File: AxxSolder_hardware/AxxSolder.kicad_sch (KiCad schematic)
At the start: 95 parts, among them IC1 LTC4440AHMS8E-5#PBF, IC2 STM32G431KBT6, IC3 TMP236AQDBZRQ1, IC4 OPA2333AIDRBR, IC5 STM32G431KBT6, IC6 TPS54302DDCR, J1 Conn_01x07_Male, J4 Conn_01x07_Male, Q2 2N7002NXAKR, U1 PEC11L-4220F-S0015, U2 BSC014N04LS

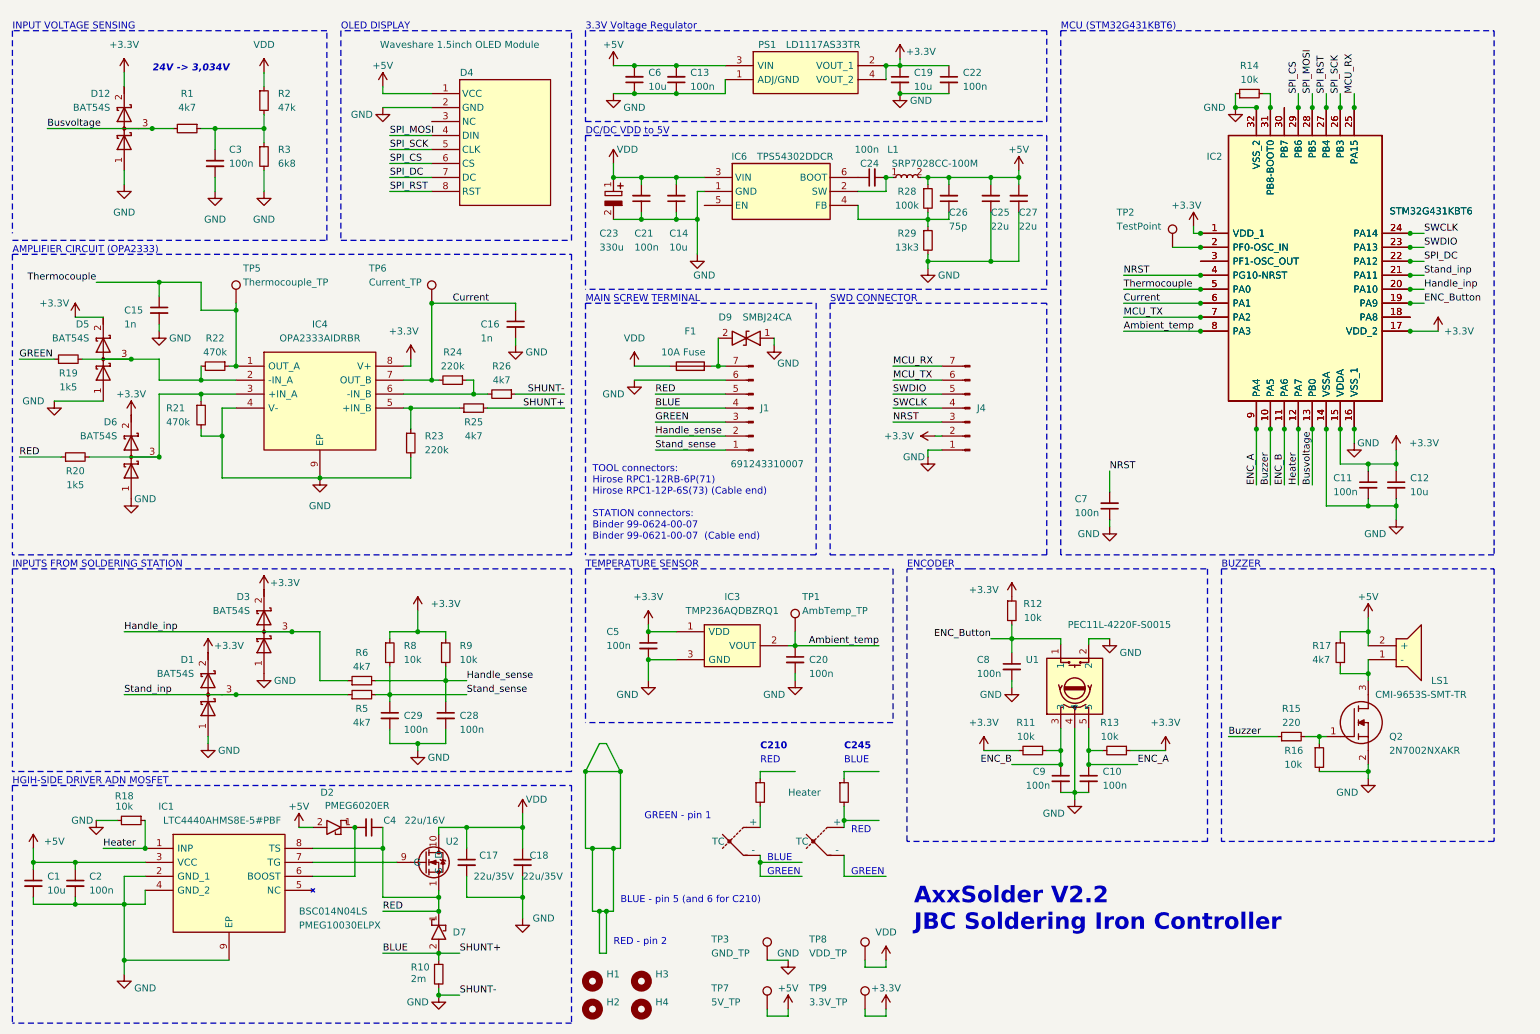
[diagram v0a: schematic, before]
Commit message: update USBC-PD branch
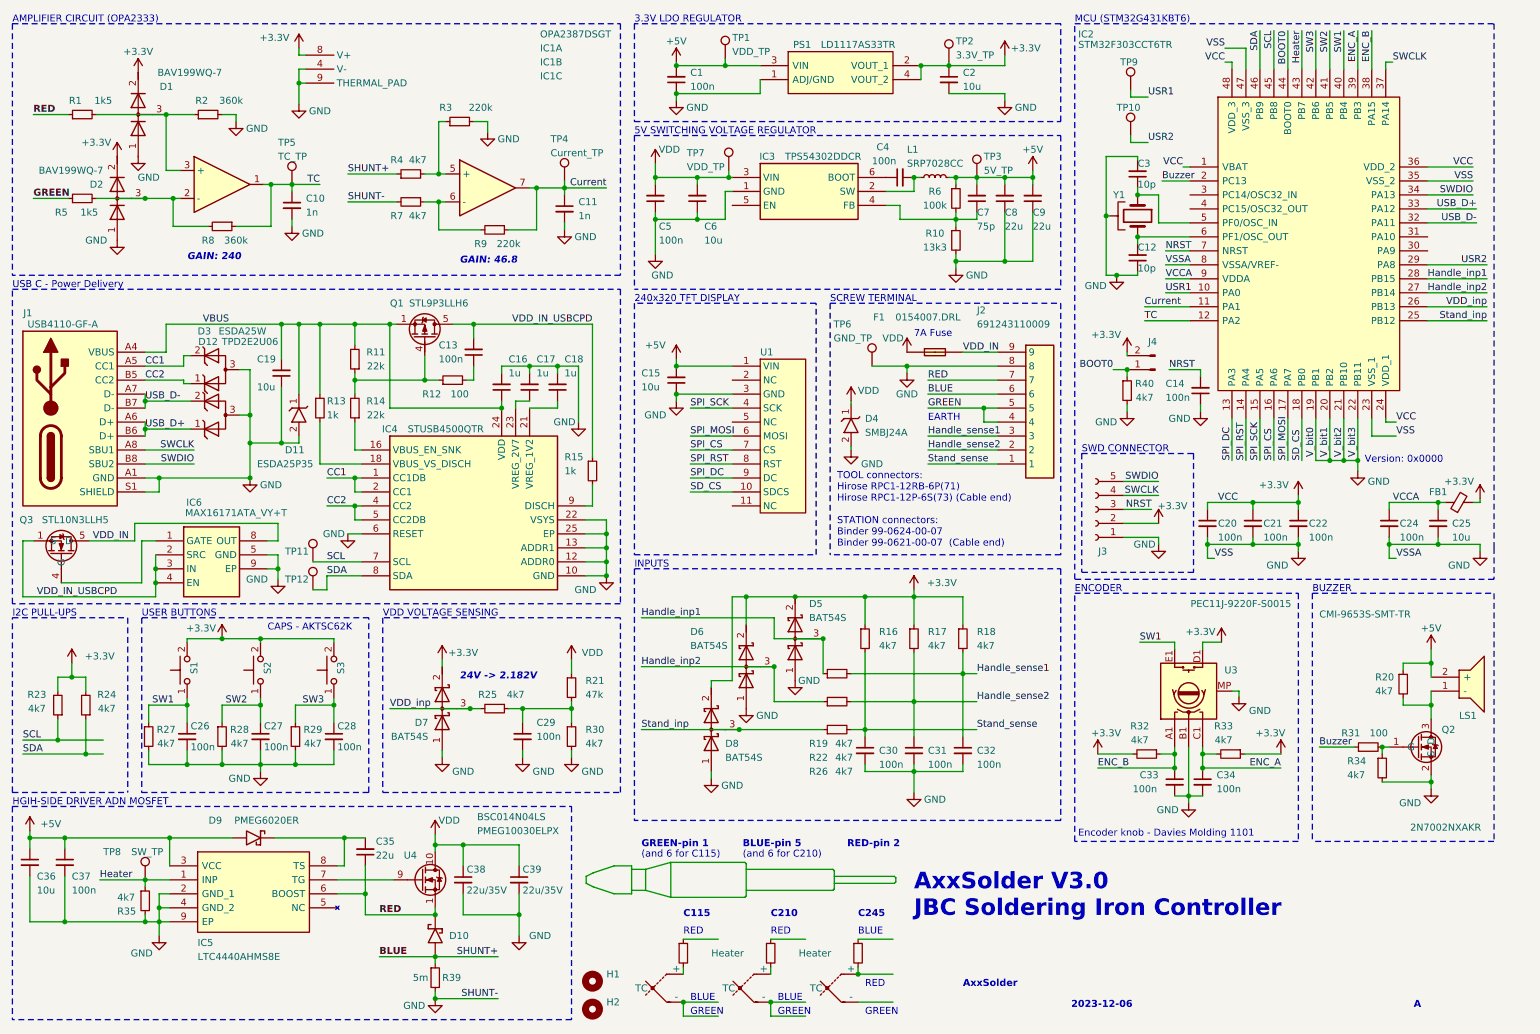
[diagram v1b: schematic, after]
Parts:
- removed C11, C5, C7, C8: 100n, Capacitor_SMD:C_0805_2012Metric, symbol Device:C_Small
- removed C23: 330u, EMZR500ARA331MJA0G:CAPAE1030X1050N, symbol EMZR500ARA331MJA0G:EMZR500ARA331MJA0G
- removed C6: 10u, Capacitor_SMD:C_0805_2012Metric, symbol Device:C_Small
- removed D4: Waveshare 1.5inch OLED Module, 1_5inch-rgb-oled-module_asm-1110:1_5inch-rgb-oled-module_asm-1110, symbol 1_5inch-rgb-oled-module_asm-1110:1_5inch-rgb-oled-module_asm-1110
- removed D6: BAT54S, BAT54S,215:SOT95P230X110-3N, symbol Device:D_Schottky_Dual_Series_AKC
- removed D9: SMBJ24CA, DIOM5436X261N, symbol SMBJ24CA:SMBJ24CA
- removed F1: 10A Fuse, 3557-2:3557-2, symbol Device:Fuse
- removed H3, H4: MountingHole, MountingHole:MountingHole_3mm, symbol Mechanical:MountingHole
- removed IC2: STM32G431KBT6, STM32G431KBT6:QFP80P900X900X160-32N, symbol STM32G431KBT6:STM32G431KBT6
- removed IC3: TMP236AQDBZRQ1, TMP236AQDBZRQ1:SOT95P237X112-3N, symbol TMP236AQDBZRQ1:TMP236AQDBZRQ1
- removed IC4: OPA2333AIDRBR, OPA2333AIDRBR:SON65P300X300X100-9N-D, symbol OPA2333AIDRBR:OPA2333AIDRBR
- removed IC5: STM32G431KBT6, Package_DFN_QFN:UFQFPN-32-1EP_5x5mm_P0.5mm_EP3.5x3.5mm, symbol STM32G431KBT6:STM32G431KBT6
- removed J1: Conn_01x07_Male, 691243310007:691243310007, symbol Connector:Conn_01x07_Male
- removed J4: Conn_01x07_Male, Connector_PinSocket_2.54mm:PinSocket_1x07_P2.54mm_Vertical, symbol Connector:Conn_01x07_Male
- removed R10: 2m, WSLP25122L500FEA:RESC6432X89N, symbol Device:R_Small
- removed R21: 470k, Resistor_SMD:R_0805_2012Metric, symbol Device:R_Small
- removed TP1: AmbTemp_TP, TestPoint:TestPoint_THTPad_D1.0mm_Drill0.5mm, symbol Connector:TestPoint
- removed TP2: TestPoint, TestPoint:TestPoint_Pad_D1.0mm, symbol Connector:TestPoint
- removed U1: PEC11L-4220F-S0015, PEC11L-4220F-S0015:PEC11L4220FS0015, symbol PEC11L-4220F-S0015:PEC11L-4220F-S0015
- added C13, C14, C21, C24, C26, C27, C28, C32: 100n, Capacitor_SMD:C_0603_1608Metric, symbol Device:C_Small
- added C15, C19, C25: 10u, Capacitor_SMD:C_0603_1608Metric, symbol Device:C_Small
- added C16, C17, C18: 1u, Capacitor_SMD:C_0603_1608Metric, symbol Device:C_Small
- added C3: 10p, Capacitor_SMD:C_0603_1608Metric, symbol Device:C_Small
- added D1, D2: BAV199WQ-7, footprints:SOT65P210X110-3N, symbol BAV199WQ-7:BAV199WQ-7
- added D11: ESDA25P35, footprints:ESDA25P351U1M, symbol ESDA25P35-1U1M:ESDA25P35-1U1M
- added D12: TPD2E2U06, footprints:SOT95P237X95-3N, symbol TPD2E2U06QDBZRQ1:TPD2E2U06QDBZRQ1
- added D3: ESDA25W, footprints:SOT65P210X110-3N, symbol ESDA25W:ESDA25W
- added D4: SMBJ24A, footprints:DIOM5436X261N, symbol SMBJ24A:SMBJ24A
- added F1: 0154007.DRL, footprints:0154100DR, symbol 0154007_DRL:0154007.DRL
- added FB1: BLM18HE601SN1D, Resistor_SMD:R_0603_1608Metric, symbol BLM18HE601SN1D:BLM18HE601SN1D
- added IC1: OPA2387DSGT, footprints:SON50P200X200X80-9N, symbol OPA2387DSGT:OPA2387DSGT
- added IC2: STM32F303CCT6TR, footprints:QFP50P900X900X160-48N, symbol STM32F303CCT6TR:STM32F303CCT6TR
- added IC4: STUSB4500QTR, footprints:QFN50P400X400X100-25N-D, symbol STUSB4500QTR:STUSB4500QTR
- added IC6: MAX16171ATA_VY+T, SON50P300X200X80-9N, symbol MAX16171ATA_VY+T:MAX16171ATA_VY+T
- added J1: USB4110-GF-A, footprints:USB4110GFA, symbol USB4110-GF-A:USB4110-GF-A
- added J2: 691243110009, footprints:691243110009, symbol 691243110009:691243110009
- added J3: Conn_01x05_Socket, Connector_PinSocket_2.54mm:PinSocket_1x05_P2.54mm_Vertical, symbol Connector:Conn_01x05_Socket
- added J4: Conn_01x02_Pin, Connector_PinHeader_1.27mm:PinHeader_1x02_P1.27mm_Vertical, symbol Connector:Conn_01x02_Pin
- added Q1: STL9P3LLH6, footprints:STL20N6F7, symbol STL9P3LLH6:STL9P3LLH6
- added Q3: STL10N3LLH5, STL10N3LLH5, symbol STL10N3LLH5:STL10N3LLH5
- added R11: 22k, Resistor_SMD:R_0603_1608Metric, symbol Device:R_Small
- added R13: 1k, Resistor_SMD:R_0603_1608Metric, symbol Device:R_Small
- added R18, R19, R23, R24, R27, R28, R29, R40: 4k7, Resistor_SMD:R_0603_1608Metric, symbol Device:R_Small
- added R2: 360k, Resistor_SMD:R_0603_1608Metric, symbol Device:R_Small
- added R31: 100, Resistor_SMD:R_0603_1608Metric, symbol Device:R_Small
- added R36: Heater, symbol Device:R_Small
- added R39: 5m, footprints:RESC6432X89N, symbol WSLP25125L000FEA:WSLP25125L000FEA
- added S1, S2, S3: ADTSM644KVTR, footprints:ADTSM644KVTR, symbol ADTSM644KVTR:ADTSM644KVTR
- added TC1: TC, symbol Device:Thermocouple
- added TP10, TP11, TP12, TP9: DIAG_TP, TestPoint:TestPoint_Pad_D1.0mm, symbol Connector:TestPoint
- added TP7: VDD_TP, TestPoint:TestPoint_THTPad_D1.0mm_Drill0.5mm, symbol Connector:TestPoint
- added TP8: SW_TP, TestPoint:TestPoint_Pad_D1.0mm, symbol Connector:TestPoint
- added U1: ~, footprints:Adafruit_240x320_TFT, symbol Adafruit_240x320_TFT:Adafruit_240x320_TFT
- added U3: PEC11J-9220F-S0015, footprints:PEC11J9220FS0015, symbol PEC11J-9220F-S0015:PEC11J-9220F-S0015
- added Y1: NX2016SA-32M-EXS00A-CS06465, footprints:NX2016SA32MEXS00ACS06465, symbol NX2016SA-32M-EXS00A-CS06465:NX2016SA-32M-EXS00A-CS06465
- C1: renamed from C13; footprint Capacitor_SMD:C_0805_2012Metric -> Capacitor_SMD:C_0603_1608Metric; Manufacturer_Name (none) -> KEMET; Manufacturer_Part_Number (none) -> C0603C104J5RACTU
- C10: renamed from C15; footprint Capacitor_SMD:C_0805_2012Metric -> Capacitor_SMD:C_0603_1608Metric; Manufacturer_Name (none) -> KEMET; Manufacturer_Part_Number (none) -> C0603C102K3GAC
- C11: renamed from C16; footprint Capacitor_SMD:C_0805_2012Metric -> Capacitor_SMD:C_0603_1608Metric; Manufacturer_Name (none) -> KEMET; Manufacturer_Part_Number (none) -> C0603C102K3GAC
- C12: value 10u -> 10p; footprint Capacitor_SMD:C_0805_2012Metric -> Capacitor_SMD:C_0603_1608Metric; Manufacturer_Name (none) -> KEMET; Manufacturer_Part_Number (none) -> C0603C100J5GAC
- C2: renamed from C19; footprint Capacitor_SMD:C_0805_2012Metric -> Capacitor_SMD:C_0603_1608Metric; Manufacturer_Name (none) -> Murata Electronics; Manufacturer_Part_Number (none) -> GRM188R6YA106MA73J
- C20, C22: footprint Capacitor_SMD:C_0805_2012Metric -> Capacitor_SMD:C_0603_1608Metric; Manufacturer_Name (none) -> KEMET; Manufacturer_Part_Number (none) -> C0603C104J5RACTU
- C29: renamed from C3; footprint Capacitor_SMD:C_0805_2012Metric -> Capacitor_SMD:C_0603_1608Metric; Manufacturer_Name (none) -> KEMET; Manufacturer_Part_Number (none) -> C0603C104J5RACTU
- C30: renamed from C29; footprint Capacitor_SMD:C_0805_2012Metric -> Capacitor_SMD:C_0603_1608Metric; Manufacturer_Name (none) -> KEMET; Manufacturer_Part_Number (none) -> C0603C104J5RACTU
- C31: renamed from C28; footprint Capacitor_SMD:C_0805_2012Metric -> Capacitor_SMD:C_0603_1608Metric; Manufacturer_Name (none) -> KEMET; Manufacturer_Part_Number (none) -> C0603C104J5RACTU
- C33: renamed from C9; footprint Capacitor_SMD:C_0805_2012Metric -> Capacitor_SMD:C_0603_1608Metric; Manufacturer_Name (none) -> KEMET; Manufacturer_Part_Number (none) -> C0603C104J5RACTU
- C34: renamed from C10; footprint Capacitor_SMD:C_0805_2012Metric -> Capacitor_SMD:C_0603_1608Metric; Manufacturer_Name (none) -> KEMET; Manufacturer_Part_Number (none) -> C0603C104J5RACTU
- C35: renamed from C4; value 22u/16V -> 22u; Manufacturer_Name (none) -> Samsung Electro-Mechanics; Manufacturer_Part_Number (none) -> CL31A226MOCLNNC
- C36: renamed from C1; footprint Capacitor_SMD:C_0805_2012Metric -> Capacitor_SMD:C_0603_1608Metric; Manufacturer_Name (none) -> Murata Electronics; Manufacturer_Part_Number (none) -> GRM188R6YA106MA73J
- C37: renamed from C2; footprint Capacitor_SMD:C_0805_2012Metric -> Capacitor_SMD:C_0603_1608Metric; Manufacturer_Name (none) -> KEMET; Manufacturer_Part_Number (none) -> C0603C104J5RACTU
- C38: renamed from C17; Manufacturer_Name (none) -> TDK; Manufacturer_Part_Number (none) -> C3216X5R1V226M160AC
- C39: renamed from C18; Manufacturer_Name (none) -> TDK; Manufacturer_Part_Number (none) -> C3216X5R1V226M160AC
- C4: renamed from C24; footprint Capacitor_SMD:C_0805_2012Metric -> Capacitor_SMD:C_0603_1608Metric; Manufacturer_Name (none) -> KEMET; Manufacturer_Part_Number (none) -> C0603C104J5RACTU
- C5: renamed from C21; footprint Capacitor_SMD:C_0805_2012Metric -> Capacitor_SMD:C_0603_1608Metric; Manufacturer_Name (none) -> KEMET; Manufacturer_Part_Number (none) -> C0603C104J5RACTU
- C6: renamed from C14; footprint Capacitor_SMD:C_0805_2012Metric -> Capacitor_SMD:C_0603_1608Metric; Manufacturer_Name (none) -> Murata Electronics; Manufacturer_Part_Number (none) -> GRM188R6YA106MA73J
- C7: renamed from C26; footprint Capacitor_SMD:C_0805_2012Metric -> Capacitor_SMD:C_0603_1608Metric; Manufacturer_Name (none) -> KEMET; Manufacturer_Part_Number (none) -> C0603C750K5HACTU
- C8: renamed from C25; Manufacturer_Name (none) -> Samsung Electro-Mechanics; Manufacturer_Part_Number (none) -> CL31A226MOCLNNC
- C9: renamed from C27; Manufacturer_Name (none) -> Samsung Electro-Mechanics; Manufacturer_Part_Number (none) -> CL31A226MOCLNNC
- D10: renamed from D7; footprint PMEG10030ELPX:SODFL4725X110N -> footprints:SODFL4725X110N
- D5: footprint BAT54S,215:SOT95P230X110-3N -> footprints:SOT95P230X110-3N; Manufacturer_Name (none) -> Diotec Semiconductor; Manufacturer_Part_Number (none) -> BAT54S; Mouser Part Number (none) -> 637-BAT54S; Mouser Price/Stock (none) -> https://www.mouser.co.uk/ProductDetail/Diotec-Semiconductor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
- D6: renamed from D3; footprint BAT54S,215:SOT95P230X110-3N -> footprints:SOT95P230X110-3N; Manufacturer_Name (none) -> Diotec Semiconductor; Manufacturer_Part_Number (none) -> BAT54S; Mouser Part Number (none) -> 637-BAT54S; Mouser Price/Stock (none) -> https://www.mouser.co.uk/ProductDetail/Diotec-Semiconductor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
- D7: renamed from D12; footprint BAT54S,215:SOT95P230X110-3N -> footprints:SOT95P230X110-3N; Manufacturer_Name (none) -> Diotec Semiconductor; Manufacturer_Part_Number (none) -> BAT54S; Mouser Part Number (none) -> 637-BAT54S; Mouser Price/Stock (none) -> https://www.mouser.co.uk/ProductDetail/Diotec-Semiconductor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
- D8: renamed from D1; footprint BAT54S,215:SOT95P230X110-3N -> footprints:SOT95P230X110-3N; Manufacturer_Name (none) -> Diotec Semiconductor; Manufacturer_Part_Number (none) -> BAT54S; Mouser Part Number (none) -> 637-BAT54S; Mouser Price/Stock (none) -> https://www.mouser.co.uk/ProductDetail/Diotec-Semiconductor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
- D9: renamed from D2; footprint PMEG6020ER,115:PMEG6020ER115 -> footprints:PMEG6020ER115
- H1, H2: footprint MountingHole:MountingHole_3mm -> MountingHole:MountingHole_2.5mm; Assembly Comment (none) -> N/A; now left out of the parts list
- IC3: renamed from IC6; footprint TPS54302DDCR:SOT95P280X110-6N -> footprints:SOT95P280X110-6N
- IC5: renamed from IC1; value LTC4440AHMS8E-5#PBF -> LTC4440AHMS8E; footprint LTC4440AHMS8E-5#PBF:SOP65P490X110-9N -> footprints:SOP65P490X110-9N
- L1: value SRP7028CC-100M -> SRP7028CC; footprint SRP7028CC-100M:INDPM7366X300N -> footprints:INDPM7366X300N; Mouser Part Number (none) -> 652-SRP7028CC-100M
- LS1: footprint CMI-9653S-SMT-TR:CMI9653SSMTTR -> footprints:CMI9653SSMTTR
- PS1: footprint SOT230P700X190-4N -> footprints:SOT230P700X190-4N
- Q2: footprint 2N7002NXAKR:SOT95P230X110-3N -> SOT95P230X110-3N
- R1: renamed from R20; footprint Resistor_SMD:R_0805_2012Metric -> Resistor_SMD:R_0603_1608Metric; Manufacturer_Name (none) -> Panasonic; Manufacturer_Part_Number (none) -> ERJ-H3ED1501V; Mouser Part Number (none) -> 667-ERJ-H3ED1501V
- R10: renamed from R29; footprint Resistor_SMD:R_0805_2012Metric -> Resistor_SMD:R_0603_1608Metric; Manufacturer_Name (none) -> Panasonic; Manufacturer_Part_Number (none) -> ERJ-PB3B1332V; Mouser Part Number (none) -> 667-ERJ-PB3B1332V
- R12: value 10k -> 100; footprint Resistor_SMD:R_0805_2012Metric -> Resistor_SMD:R_0603_1608Metric; Manufacturer_Name (none) -> Panasonic; Manufacturer_Part_Number (none) -> ERJ-P03F1000V; Mouser Part Number (none) -> 667-ERJ-P03F1000V
- R14: value 10k -> 22k; footprint Resistor_SMD:R_0805_2012Metric -> Resistor_SMD:R_0603_1608Metric; Manufacturer_Name (none) -> Panasonic; Manufacturer_Part_Number (none) -> ERJ-UP3J223V; Mouser Part Number (none) -> 667-ERJ-UP3J223V
- R15: value 220 -> 1k; footprint Resistor_SMD:R_0805_2012Metric -> Resistor_SMD:R_0603_1608Metric; Manufacturer_Name (none) -> Panasonic; Manufacturer_Part_Number (none) -> ERJ-H3EF1001V; Mouser Part Number (none) -> 667-ERJ-H3EF1001V
- R16: renamed from R8; value 10k -> 4k7; footprint Resistor_SMD:R_0805_2012Metric -> Resistor_SMD:R_0603_1608Metric; Manufacturer_Name (none) -> Panasonic; Manufacturer_Part_Number (none) -> ERJ-3RBD4701V; Mouser Part Number (none) -> 667-ERJ-3RBD4701V
- R17: renamed from R9; value 10k -> 4k7; footprint Resistor_SMD:R_0805_2012Metric -> Resistor_SMD:R_0603_1608Metric; Manufacturer_Name (none) -> Panasonic; Manufacturer_Part_Number (none) -> ERJ-3RBD4701V; Mouser Part Number (none) -> 667-ERJ-3RBD4701V
- R20: renamed from R17; footprint Resistor_SMD:R_0805_2012Metric -> Resistor_SMD:R_0603_1608Metric; Manufacturer_Name (none) -> Panasonic; Manufacturer_Part_Number (none) -> ERJ-3RBD4701V; Mouser Part Number (none) -> 667-ERJ-3RBD4701V
- R21: renamed from R2; footprint Resistor_SMD:R_0805_2012Metric -> Resistor_SMD:R_0603_1608Metric; Manufacturer_Name (none) -> Panasonic; Manufacturer_Part_Number (none) -> ERJ-H3ED4702V; Mouser Part Number (none) -> 667-ERJ-H3ED4702V
- R22: renamed from R6; footprint Resistor_SMD:R_0805_2012Metric -> Resistor_SMD:R_0603_1608Metric; Manufacturer_Name (none) -> Panasonic; Manufacturer_Part_Number (none) -> ERJ-3RBD4701V; Mouser Part Number (none) -> 667-ERJ-3RBD4701V
- R25: renamed from R1; footprint Resistor_SMD:R_0805_2012Metric -> Resistor_SMD:R_0603_1608Metric; Manufacturer_Name (none) -> Panasonic; Manufacturer_Part_Number (none) -> ERJ-3RBD4701V; Mouser Part Number (none) -> 667-ERJ-3RBD4701V
- R26: renamed from R5; footprint Resistor_SMD:R_0805_2012Metric -> Resistor_SMD:R_0603_1608Metric; Manufacturer_Name (none) -> Panasonic; Manufacturer_Part_Number (none) -> ERJ-3RBD4701V; Mouser Part Number (none) -> 667-ERJ-3RBD4701V
- R3: renamed from R23; footprint Resistor_SMD:R_0805_2012Metric -> Resistor_SMD:R_0603_1608Metric; Manufacturer_Name (none) -> Panasonic; Manufacturer_Part_Number (none) -> ERJ-3RED2203V; Mouser Part Number (none) -> 667-ERJ-3RED2203V
- R30: renamed from R3; value 6k8 -> 4k7; footprint Resistor_SMD:R_0805_2012Metric -> Resistor_SMD:R_0603_1608Metric; Manufacturer_Name (none) -> Panasonic; Manufacturer_Part_Number (none) -> ERJ-3RBD4701V; Mouser Part Number (none) -> 667-ERJ-3RBD4701V
- R32: renamed from R11; value 10k -> 4k7; footprint Resistor_SMD:R_0805_2012Metric -> Resistor_SMD:R_0603_1608Metric; Manufacturer_Name (none) -> Panasonic; Manufacturer_Part_Number (none) -> ERJ-3RBD4701V; Mouser Part Number (none) -> 667-ERJ-3RBD4701V
- R33: renamed from R13; value 10k -> 4k7; footprint Resistor_SMD:R_0805_2012Metric -> Resistor_SMD:R_0603_1608Metric; Manufacturer_Name (none) -> Panasonic; Manufacturer_Part_Number (none) -> ERJ-3RBD4701V; Mouser Part Number (none) -> 667-ERJ-3RBD4701V
- R34: renamed from R16; value 10k -> 4k7; footprint Resistor_SMD:R_0805_2012Metric -> Resistor_SMD:R_0603_1608Metric; Manufacturer_Name (none) -> Panasonic; Manufacturer_Part_Number (none) -> ERJ-3RBD4701V; Mouser Part Number (none) -> 667-ERJ-3RBD4701V
- R35: renamed from R18; value 10k -> 4k7; footprint Resistor_SMD:R_0805_2012Metric -> Resistor_SMD:R_0603_1608Metric; Manufacturer_Name (none) -> Panasonic; Manufacturer_Part_Number (none) -> ERJ-3RBD4701V; Mouser Part Number (none) -> 667-ERJ-3RBD4701V
- R37: renamed from R4; Assembly Comment (none) -> N/A
- R38: renamed from R7; Assembly Comment (none) -> N/A
- R4: renamed from R25; footprint Resistor_SMD:R_0805_2012Metric -> Resistor_SMD:R_0603_1608Metric; Manufacturer_Name (none) -> Panasonic; Manufacturer_Part_Number (none) -> ERJ-3RBD4701V; Mouser Part Number (none) -> 667-ERJ-3RBD4701V
- R5: renamed from R19; footprint Resistor_SMD:R_0805_2012Metric -> Resistor_SMD:R_0603_1608Metric; Manufacturer_Name (none) -> Panasonic; Manufacturer_Part_Number (none) -> ERJ-H3ED1501V; Mouser Part Number (none) -> 667-ERJ-H3ED1501V
- R6: renamed from R28; footprint Resistor_SMD:R_0805_2012Metric -> Resistor_SMD:R_0603_1608Metric; Manufacturer_Name (none) -> Panasonic; Manufacturer_Part_Number (none) -> ERJ-UP3D1003V; Mouser Part Number (none) -> 667-ERJ-UP3D1003V
- R7: renamed from R26; footprint Resistor_SMD:R_0805_2012Metric -> Resistor_SMD:R_0603_1608Metric; Manufacturer_Name (none) -> Panasonic; Manufacturer_Part_Number (none) -> ERJ-3RBD4701V; Mouser Part Number (none) -> 667-ERJ-3RBD4701V
- R8: renamed from R22; value 470k -> 360k; footprint Resistor_SMD:R_0805_2012Metric -> Resistor_SMD:R_0603_1608Metric; Manufacturer_Name (none) -> Panasonic; Manufacturer_Part_Number (none) -> ERJ-3RED3603V; Mouser Part Number (none) -> 667-ERJ-3RED3603V
- R9: renamed from R24; footprint Resistor_SMD:R_0805_2012Metric -> Resistor_SMD:R_0603_1608Metric; Manufacturer_Name (none) -> Panasonic; Manufacturer_Part_Number (none) -> ERJ-3RED2203V; Mouser Part Number (none) -> 667-ERJ-3RED2203V
- TC2: renamed from TC1; Assembly Comment (none) -> N/A
- TC3: renamed from TC2; Assembly Comment (none) -> N/A
- TP1: renamed from TP8; Assembly Comment (none) -> N/A; now left out of the parts list
- TP2: renamed from TP9; Assembly Comment (none) -> N/A; now left out of the parts list
- TP3: renamed from TP7; Assembly Comment (none) -> N/A; now left out of the parts list
- TP4: renamed from TP6; Assembly Comment (none) -> N/A; now left out of the parts list
- TP5: value Thermocouple_TP -> TC_TP; Assembly Comment (none) -> N/A; now left out of the parts list
- TP6: renamed from TP3; Assembly Comment (none) -> N/A; now left out of the parts list
- U4: renamed from U2; footprint BSC014N04LS:BSC014N04LS -> footprints:BSC014N04LS; Manufacturer_Name (none) -> Infineon Technologies; Manufacturer_Part_Number (none) -> BSC014N04LSATMA1; Mouser Part Number (none) -> 726-BSC014N04LSATMA1
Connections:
- net Ambient_temp is gone; now on net +3.3V: C20.1
- net +3.3V: now also C21.1, D1.2, D2.2, FB1.2, IC1.8 (V+), IC2.1 (VBAT), IC2.24 (VDD_1), IC2.36 (VDD_2), IC2.48 (VDD_3), J3.2 (Pin_2), J4.2 (Pin_2), R18.1, R23.2, R24.2, S1.2, S2.2, S3.2, U3.D1; no longer C12.1, R12.1
- net +5V: now also TP1.1, C15.2, U1.1 (VIN)
- net BLUE: now also R4.1, J2.6, R39.1; no longer R4.2
- net Buzzer: now also IC2.2 (PC13), R31.1; no longer R15.1
- net Current: now also R9.1, IC1.7, IC2.11 (PA1); no longer R9.2
- net ENC_A: now also IC2.39 (PB3), U3.C1
- net ENC_B: now also IC2.38 (PA15), U3.A1
- net GND: now also C12.1, R7.2, C14.1, C15.1, C16.2, C17.2, C18.2, C19.1, C21.2, C24.2, C25.2, C26.2, C27.2, C28.2, C3.2, C32.2, D1.1, D11.2 (A), D12.3, D2.1, D3.3, D4.2 (A), IC1.4 (V-), IC1.9 (THERMAL_PAD), IC2.19 (PB1), IC2.20 (PB2), IC2.21 (PB10), IC2.22 (PB11), IC2.23 (VSS_1), IC2.35 (VSS_2), IC2.47 (VSS_3), IC2.8 (VSSA/VREF-), IC4.10 (GND), IC4.12 (ADDR0), IC4.13 (ADDR1), IC4.22 (VSYS), IC4.25 (EP), IC4.6 (RESET), IC6.5 (GND), IC6.9 (EP), J1.A1 (GND), J1.A12 (GND), J1.B1 (GND), J1.B12 (GND), J1.S1 (SHIELD), J2.8, J3.1 (Pin_1), R2.2, R27.2, R28.2, R29.2, R39.2, R40.2, U1.3 (GND), U3.B1, U3.MP, Y1.2; no longer C12.2, R14.1, R7.1
- net GREEN: now also J2.4, J2.5
- net Heater: now also IC2.43 (PB7), TP8.1
- net NRST: now also C14.2, IC2.7 (NRST), J3.3 (Pin_3)
- net RED: now also IC5.6 (BOOST), J2.7; no longer IC5.8 (TS)
- net SPI_CS: now also IC2.16 (PA6), U1.7 (CS)
- net SPI_DC: now also IC2.13 (PA3), U1.9 (DC)
- net SPI_MOSI: now also IC2.17 (PA7), U1.6 (MOSI)
- net SPI_RST: now also IC2.14 (PA4), U1.8 (RST)
- net SPI_SCK: now also IC2.15 (PA5), U1.4 (SCK)
- net SWCLK: now also IC2.37 (PA14), J1.A8 (SBU1), J3.4 (Pin_4)
- net SWDIO: now also IC2.34 (PA13), J1.B8 (SBU2), J3.5 (Pin_5)
- net Stand_inp: now also IC2.25 (PB12)
- net Stand_sense: now also J2.1
- net VDD: now also D4.1 (K), F1.1, TP7.1; no longer TP1.1
- net at Q2.1 (G), R34.1: now also R31.2; no longer R15.2
- net at R5.2, R8.2: now also D2.3, IC1.2 (-); no longer D5.3 (common)
- net at R1.2: now also D1.3, IC1.3 (+), R2.1
- net at R3.1: now also R4.2, IC1.5 (+); no longer R4.1
- net at R14.2: now also R12.1, Q1.4 (G), R11.1
- net at C35.2, D9.1: now also IC5.8 (TS); no longer IC5.6 (BOOST)
- net Busvoltage renamed VDD_inp
- net VDD_inp: now also IC2.26 (PB13)
- net ENC_Button: no longer names the net of R12.2
- net ENC_Button: now also C13.1
- net Handle_inp renamed Handle_inp2
- net Handle_inp2: now also IC2.27 (PB14)
- net Handle_sense renamed Handle_sense2
- net Handle_sense2: now also J2.2
- net Thermocouple renamed TC
- net TC: now also IC1.1, IC2.12 (PA2)
- new net: R36.2, TC1.1 (+)
- new net: IC4.18 (VBUS_VS_DISCH), R13.2
- new net: IC6.1 (GATE), Q3.4 (G)
- new net: C17.1, IC4.23 (VREG_2V7)
- new net: IC1.6 (-), R7.1, R9.2
- new net: C12.2, IC2.6 (PF1/OSC_OUT), Y1.3
- new net: C3.1, IC2.5 (PF0/OSC_IN), Y1.1
- new net: C18.1, IC4.21 (VREG_1V2)
- new net: IC4.16 (VBUS_EN_SNK), R14.1
- new net: IC4.9 (DISCH), R15.2
- new net BOOT0: IC2.44 (BOOT0), J4.1 (Pin_1), R40.1
- new net CC1: D3.2, IC4.1 (CC1DB), IC4.2 (CC1), J1.A5 (CC1)
- new net CC2: D3.1, IC4.4 (CC2), IC4.5 (CC2DB), J1.B5 (CC2)
- new net Handle_inp1: D5.3 (common), IC2.28 (PB15), R19.1
- new net Handle_sense1: C32.1, J2.3, R18.2, R19.2
- new net SCL: IC2.45 (PB8), IC4.7 (SCL), R23.1, TP11.1
- new net SDA: IC2.46 (PB9), IC4.8 (SDA), R24.1, TP12.1
- new net SD_CS: IC2.18 (PB0), U1.10 (SDCS)
- new net SW1: C26.1, IC2.40 (PB4), R27.1, S1.1, U3.E1
- new net SW2: C27.1, IC2.41 (PB5), R28.1, S2.1
- new net SW3: C28.1, IC2.42 (PB6), R29.1, S3.1
- new net USB_D+: D12.1, IC2.33 (PA12), J1.A6 (D+), J1.B6 (D+)
- new net USB_D-: D12.2, IC2.32 (PA11), J1.A7 (D-), J1.B7 (D-)
- new net USR1: IC2.10 (PA0), TP9.1
- new net USR2: IC2.29 (PA8), TP10.1
- new net VBUS: C16.1, C19.2, D11.1 (K), IC4.24 (VDD), J1.A4 (VBUS), J1.A9 (VBUS), J1.B4 (VBUS), J1.B9 (VBUS), Q1.1 (S), R11.2, R13.1
- new net VCCA: C24.1, C25.1, FB1.1, IC2.9 (VDDA)
- new net VDD_IN: F1.2, IC6.8 (OUT), J2.9, Q3.5 (D)
- new net VDD_IN_USBCPD: C13.2, IC6.2 (SRC), IC6.3 (IN), IC6.4 (EN), Q1.5 (D), Q3.1 (S), R15.1
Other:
- note added: "(and 6 for C115)"
- note added: "(and 6 for C210)"
- note added: "2023-12-06"
- note added: "240x320 TFT DISPLAY"
- note added: "24V -> 2.182V"
- note added: "3.3V LDO REGULATOR"
- note added: "5V SWITCHING VOLTAGE REGULATOR"
- note added: "7A Fuse"
- note added: "A"
- note added: "AxxSolder"
- note added: "AxxSolder V3.0 JBC Soldering Iron Controller"
- note added: "BLUE-pin 5"
- note added: "C115"
- note added: "CAPS - AKTSC62K"
- note added: "EARTH"
- note added: "Encoder knob - Davies Molding 1101"
- note added: "GAIN: 240"
- note added: "GAIN: 46.8"
- note added: "GREEN-pin 1"
- note added: "I2C PULL-UPS"
- note added: "INPUTS"
- note added: "RED-pin 2"
- note added: "SCREW TERMINAL"
- note added: "USB C - Power Delivery"
- note added: "USER BUTTONS"
- note added: "VDD VOLTAGE SENSING"
- note added: "Version: 0x0000"
- note removed: "24V -> 3,034V"
- note removed: "3.3V Voltage Regulator"
- note removed: "AxxSolder V2.2 JBC Soldering Iron Controller"
- note removed: "BLUE - pin 5 (and 6 for C210)"
- note removed: "DC/DC VDD to 5V"
- note removed: "GREEN - pin 1"
- note removed: "INPUT VOLTAGE SENSING"
- note removed: "INPUTS FROM SOLDERING STATION"
- note removed: "MAIN SCREW TERMINAL"
- note removed: "OLED DISPLAY"
- note removed: "RED - pin 2"
- note removed: "TEMPERATURE SENSOR"
- moved on the sheet: C10, C11, C2, C29, C30, C31, C33, C34, C35, C36, C37, C38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

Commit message: updates in hardware and software
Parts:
- removed C12, C3: 10p, Capacitor_SMD:C_0603_1608Metric, symbol Device:C_Small
- removed C15: 10u, Capacitor_SMD:C_0603_1608Metric, symbol Device:C_Small
- removed D10: PMEG10030ELPX, footprints:SODFL4725X110N, symbol PMEG10030ELPX:PMEG10030ELPX
- removed IC2: STM32F303CCT6TR, footprints:QFP50P900X900X160-48N, symbol STM32F303CCT6TR:STM32F303CCT6TR
- removed J4: Conn_01x02_Pin, Connector_PinHeader_1.27mm:PinHeader_1x02_P1.27mm_Vertical, symbol Connector:Conn_01x02_Pin
- removed R40: 4k7, Resistor_SMD:R_0603_1608Metric, symbol Device:R_Small
- removed Y1: NX2016SA-32M-EXS00A-CS06465, footprints:NX2016SA32MEXS00ACS06465, symbol NX2016SA-32M-EXS00A-CS06465:NX2016SA-32M-EXS00A-CS06465
- added D13: PMEG6020ER, footprints:PMEG6020ER115, symbol PMEG6020ER_115:PMEG6020ER,115
- added IC7: STM32G431CBT6, QFP50P900X900X160-48N, symbol STM32G431CBT6:STM32G431CBT6
- added R41: 22k, Resistor_SMD:R_0603_1608Metric, symbol Device:R_Small
- added TP13, TP15: DIAG_TP, TestPoint:TestPoint_Pad_D1.0mm, symbol Connector:TestPoint
- added TP14: TC_TP, TestPoint:TestPoint_Pad_D1.0mm, symbol Connector:TestPoint
- C16, C17, C18: value 1u -> 10u
- IC6: footprint SON50P300X200X80-9N -> footprints:SON50P300X200X80-9N
- Q2: footprint SOT95P230X110-3N -> footprints:SOT95P230X110-3N
- Q3: footprint STL10N3LLH5 -> footprints:STL10N3LLH5
- R10: value 13k3 -> 22k
- R13, R15: value 1k -> 1k5
- R21: value 47k -> 22k
- R6: value 100k -> 220k
- TP1: value VDD_TP -> DIAG_TP; footprint TestPoint:TestPoint_THTPad_D1.0mm_Drill0.5mm -> TestPoint:TestPoint_Pad_D1.0mm
- TP6: footprint TestPoint:TestPoint_THTPad_D1.0mm_Drill0.5mm -> TestPoint:TestPoint_THTPad_D2.0mm_Drill1.0mm
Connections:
- net +3.3V: now also U1.2 (3V3), IC7.1 (VBAT), IC7.24 (VDD_1), IC7.36 (VDD_2), IC7.48 (VDD_3)
- net BLUE: now also D13.2
- net Buzzer: now also IC7.44 (PB7)
- net ENC_A: now also IC7.39 (PA15)
- net ENC_B: now also IC7.40 (PB3)
- net GND: now also IC7.19 (VSSA), IC7.2 (PC13), IC7.23 (VSS_1), IC7.3 (PC14_-_OSC32_IN), IC7.35 (VSS_2), IC7.4 (PC15_-_OSC32_OUT), IC7.47 (VSS_3), TP14.1
- net Handle_inp1: now also IC7.12 (PA4)
- net Handle_inp2: now also IC7.13 (PA5)
- net Heater: now also IC7.5 (PF0_-_OSC_IN)
- net NRST: now also IC7.7 (PG10_-_NRST)
- net RED: now also D13.1
- net SCL: now also IC7.45 (PB8-BOOT0)
- net SDA: now also IC7.46 (PB9)
- net SD_CS: now also IC7.22 (PB10)
- net SPI_CS: now also IC7.28 (PB14)
- net SPI_DC: now also IC7.25 (PB11)
- net SPI_MOSI: now also IC7.29 (PB15)
- net SPI_RST: now also IC7.26 (PB12)
- net SPI_SCK: now also IC7.27 (PB13)
- net SW1: now also IC7.42 (PB5)
- net SW2: now also IC7.32 (PA10)
- net SW3: now also IC7.30 (PA8)
- net SWCLK: now also J1.B8 (SBU2), IC7.38 (PA14); no longer J1.A8 (SBU1)
- net SWDIO: now also J1.A8 (SBU1), IC7.37 (PA13); no longer J1.B8 (SBU2)
- net Stand_inp: now also IC7.14 (PA6)
- net TC: now also IC7.11 (PA3)
- net USB_D+: now also IC7.34 (PA12)
- net USB_D-: now also IC7.33 (PA11)
- net USR1: now also IC7.15 (PA7)
- net USR2: now also IC7.16 (PB0)
- net VCCA: now also IC7.20 (VREF+), IC7.21 (VDDA)
- net VDD: now also R41.1; no longer R21.1
- net +5V renamed +6V
- net +6V: no longer TP1.1, U1.1 (VIN)
- net Current renamed CURRENT
- net CURRENT: now also IC7.10 (PA2)
- net VDD_inp renamed VBUS_IN
- net VBUS_IN: now also IC7.6 (PF1_-_OSC_OUT)
- new net: R21.1, R41.2
- new net GROUND_DET: IC7.8 (PA0), TP15.1
- new net USART_TX: IC7.31 (PA9)
- new net USR3: IC7.17 (PB1), TP1.1
- new net USR4: IC7.18 (PB2), TP13.1
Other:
- note added: "6V SWITCHING VOLTAGE REGULATOR"
- note added: "ADTSM644RVTR"
- note added: "CAPS: B32-2000"
- note added: "MCU"
- note added: "Out: 6.55V"
- note added: "PEC11J-9215F-H0015"
- note removed: "5V SWITCHING VOLTAGE REGULATOR"
- note removed: "CAPS - AKTSC62K"
- note removed: "MCU (STM32G431KBT6)"
- moved on the sheet: C14, R15, R21, TP10, TP9
